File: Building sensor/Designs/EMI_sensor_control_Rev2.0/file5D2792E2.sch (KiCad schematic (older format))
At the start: 36 parts, among them J2 Conn_02x07_Odd_Even, J3 DB9_Female, SW2 SW_Push, U16 STM32F412ZETx, Y1 ECS-3963-400-BN-TR

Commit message: overdue backup
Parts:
- removed R62: R 10k, Resistor_SMD:R_1206_3216Metric_Pad1.42x1.75mm_HandSolder, symbol Device:R
- removed U16: STM32F412ZETx, Package_QFP:LQFP-144_20x20mm_P0.5mm, symbol MCU_ST_STM32F4:STM32F412ZETx
- removed Y1: ECS-3963-400-BN-TR, ECS-3963-400-BN-TR:OSC_ECS-3963-400-BN-TR, symbol ECS-3963-400-BN-TR:ECS-3963-400-BN-TR
- added D?: LED Stat 1, LED_SMD:LED_1206_3216Metric_Pad1.42x1.75mm_HandSolder, symbol Device:LED
- added J?: Micro_SD_Card, symbol Connector:Micro_SD_Card
- added R?: R 1.2k, Resistor_SMD:R_1206_3216Metric_Pad1.42x1.75mm_HandSolder, symbol Device:R
- added U?: STM32F746VGTx, Package_QFP:LQFP-100_14x14mm_P0.5mm, symbol MCU_ST_STM32F7:STM32F746VGTx
- D6: value LED -> LED Stat 0
- R68: value R 100 -> R 1.2k
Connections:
- net labels removed: +5V, FPGA_CDONE, FPGA_CLK, FPGA_Config, FPGA_MISO, FPGA_MOSI, FPGA_SS, GNDS, MCLK, TX_On, VCP_Rx, VCP_Tx
- wire segments 236 -> 213
- no-connect marks 104 -> 10
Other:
- moved on the sheet: D6, R68

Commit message: backup
2/04/2020
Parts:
- removed C79, C82, C85: C 100n, Capacitor_SMD:C_0603_1608Metric_Pad1.05x0.95mm_HandSolder, symbol Device:C
- removed R63, R64: R 10k, Resistor_SMD:R_1206_3216Metric_Pad1.42x1.75mm_HandSolder, symbol Device:R
- C67: value C 10u -> C 100n
- C71: value C 10n -> C 100n
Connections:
- net labels added: IMon, SD_CK, SD_CMD, SD_D0, SD_D1, SD_D2, SD_D3, VCP_Rx, VCP_Tx
- net labels removed: VDD1, VDD10, VDD11, VDD2, VDD3, VDD4, VDD5, VDD6, VDD7, VDD8, VDD9, VDDUSB
- wire segments 213 -> 202
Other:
- moved on the sheet: C67, C68, C69, C70, C71, C72, C73, C74, C75, C76, C77, C78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

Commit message: Back up
Backup of rev 2.0 for board
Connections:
- net labels added: RCS, RMISO, RMOSI, RSCK, RSET_AD, RSET_CD
- wire segments 202 -> 208
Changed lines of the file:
@@
 Wire Wire Line
 	8650 6450 8650 6150
+Text GLabel 9250 7400 3    50   Input ~ 0
+RSET_CD
+Wire Wire Line
+	9250 7400 9250 7100
+Text GLabel 9100 7400 3    50   Input ~ 0
+RSET_AD
+Wire Wire Line
+	9100 7400 9100 7100
+Text GLabel 8900 7400 3    50   Input ~ 0
+RMOSI
+Text GLabel 9000 7400 3    50   Input ~ 0
+RMISO
+Text GLabel 8800 7400 3    50   Input ~ 0
+RCS
+Text GLabel 8700 7400 3    50   Input ~ 0
+RSCK
+Wire Wire Line
+	8700 7250 8700 7400
+Wire Wire Line
+	8800 7250 8800 7400
+Wire Wire Line
+	8900 7250 8900 7400
+Wire Wire Line
+	9000 7250 9000 7400
 $EndSCHEMATC

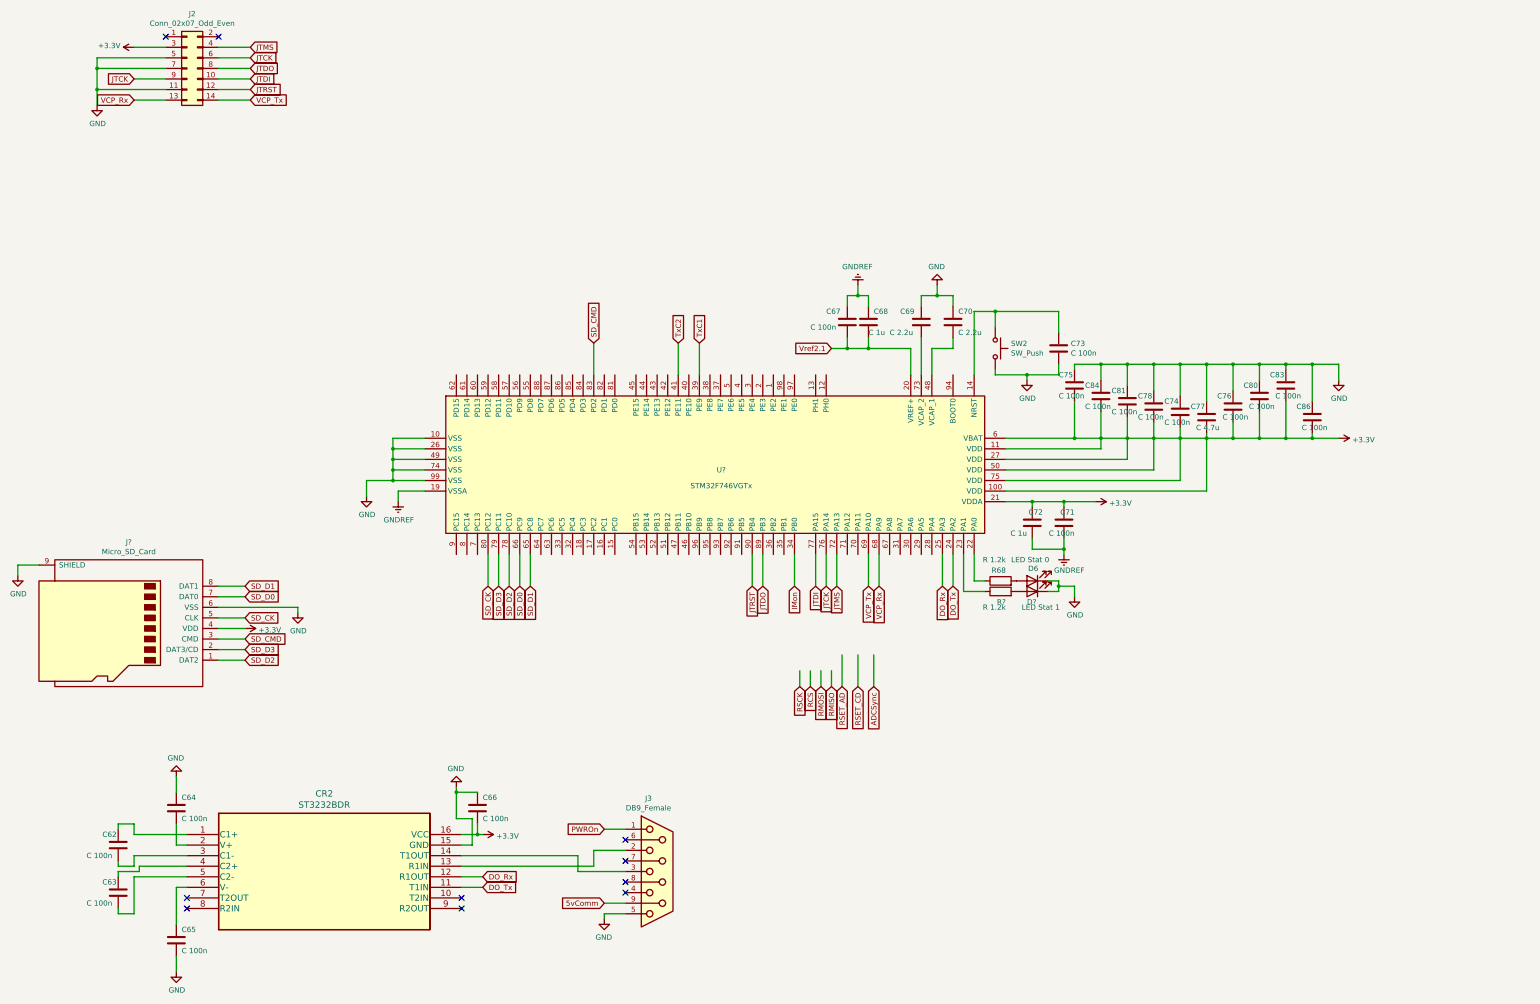
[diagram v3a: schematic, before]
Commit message: Rev 2.0 Complete
Rev 2.0 of PCB Completed
SCHM, PCB layout, and gerber files generated
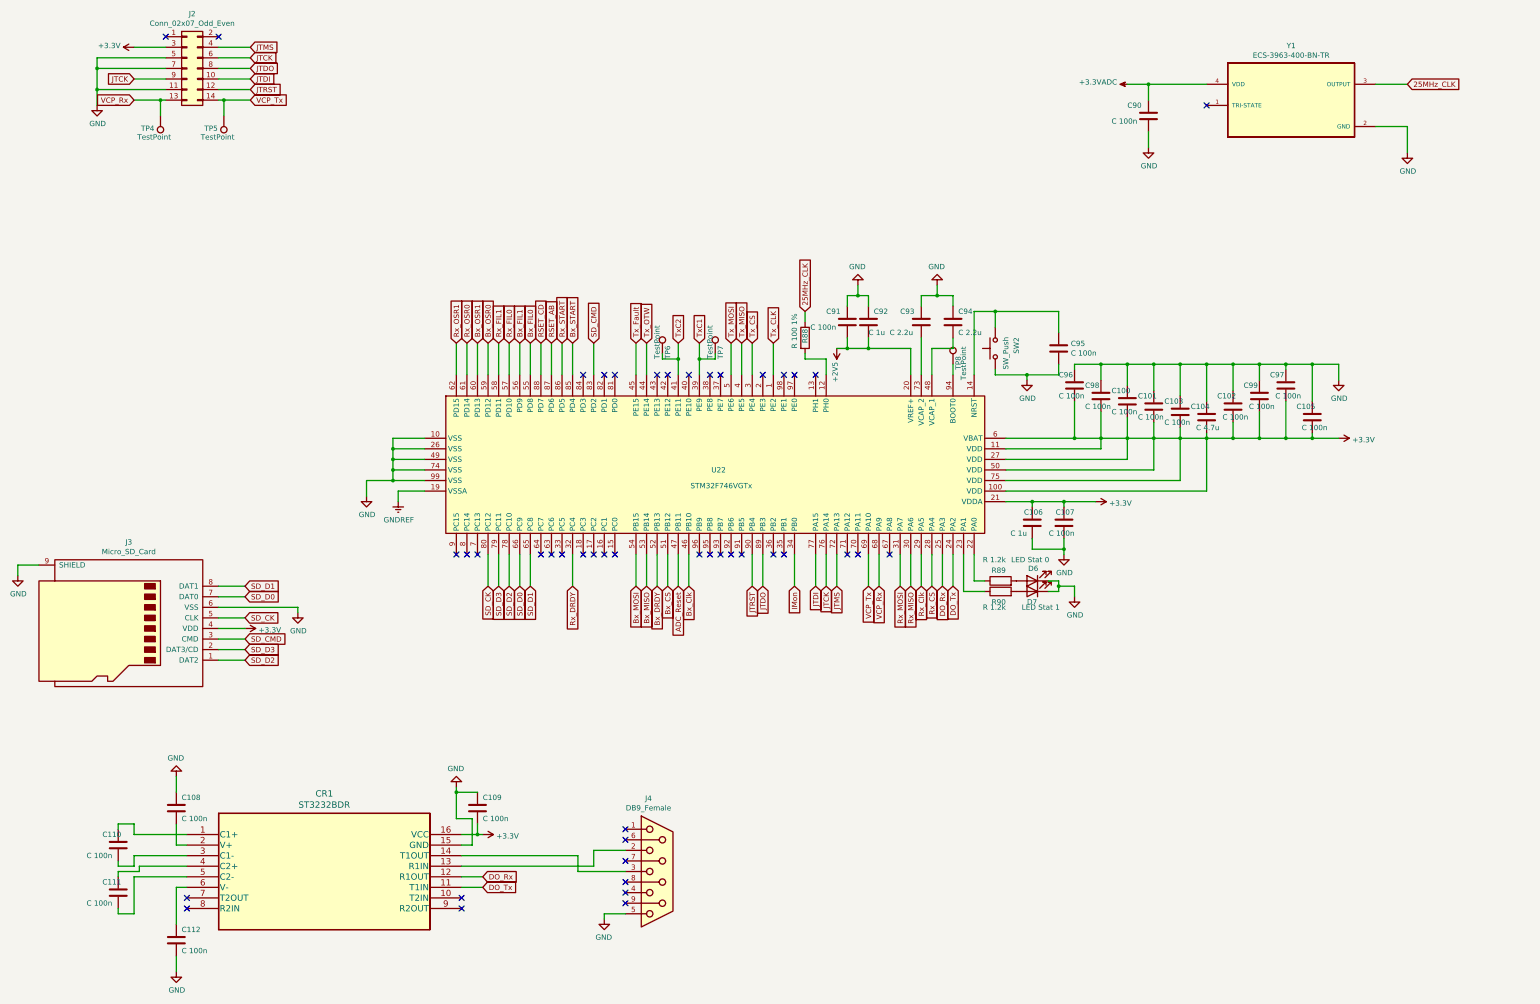
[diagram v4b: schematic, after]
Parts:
- added C90: C 100n, Capacitor_SMD:C_0603_1608Metric_Pad1.05x0.95mm_HandSolder, symbol Device:C
- added R88: R 100 1%, Resistor_SMD:R_1206_3216Metric_Pad1.42x1.75mm_HandSolder, symbol Device:R
- added TP4, TP5, TP6, TP7, TP8: TestPoint, TestPoint:TestPoint_Pad_D3.0mm, symbol Connector:TestPoint
- added Y1: ECS-3963-400-BN-TR, ECS-3963-400-BN-TR:OSC_ECS-3963-400-BN-TR, symbol ECS-3963-400-BN-TR:ECS-3963-400-BN-TR
- C107: renamed from C71; footprint Capacitor_SMD:C_0805_2012Metric_Pad1.15x1.40mm_HandSolder -> Capacitor_SMD:C_0603_1608Metric_Pad1.05x0.95mm_HandSolder
- C91: renamed from C67; footprint Capacitor_SMD:C_1210_3225Metric_Pad1.42x2.65mm_HandSolder -> Capacitor_SMD:C_0603_1608Metric_Pad1.05x0.95mm_HandSolder
- CR1: renamed from CR2; footprint footprints:ST3232BDR -> SamacSys_Parts:SOIC127P600X175-16N
- J3: renamed from J?; footprint (none) -> SamacSys_Parts:47571-0001
- R89: renamed from R68; footprint Resistor_SMD:R_1206_3216Metric_Pad1.42x1.75mm_HandSolder -> Resistor_SMD:R_0805_2012Metric_Pad1.15x1.40mm_HandSolder
- R90: renamed from R?; footprint Resistor_SMD:R_1206_3216Metric_Pad1.42x1.75mm_HandSolder -> Resistor_SMD:R_0805_2012Metric_Pad1.15x1.40mm_HandSolder
- gave numbers to parts that had none: 2
- renumbered C81 to C100, C78 to C101, C76 to C102, C74 to C103, C77 to C104, C86 to C105, C72 to C106, C64 to C108, C66 to C109, C62 to C110, C63 to C111, C65 to C112, C68 to C92, C69 to C93, C70 to C94, C73 to C95, C75 to C96, C83 to C97, C84 to C98, C80 to C99, J3 to J4
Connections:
- net labels added: +2V5, +3.3VADC, 25MHz_CLK, ADC_Reset, Bx_CS, Bx_Clk, Bx_DRDY, Bx_FIL0, Bx_FIL1, Bx_MISO, Bx_MOSI, Bx_OSR0, Bx_OSR1, Bx_START, RSET_AB, Rx_CS, Rx_Clk, Rx_DRDY, Rx_FIL0, Rx_FIL1, Rx_MISO, Rx_MOSI, Rx_OSR0, Rx_OSR1, Rx_START, Tx_CLK, Tx_CS, Tx_Fault, Tx_MISO, Tx_MOSI, Tx_OTW
- net labels removed: 5vComm, ADCSync, PWROn, RCS, RMISO, RMOSI, RSCK, RSET_AD, Vref2.1
- wire segments 208 -> 250
- no-connect marks 10 -> 45
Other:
- moved on the sheet: SW2
